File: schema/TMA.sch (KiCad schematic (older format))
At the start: 20 parts, among them U1 BMP280, U2 BMI160

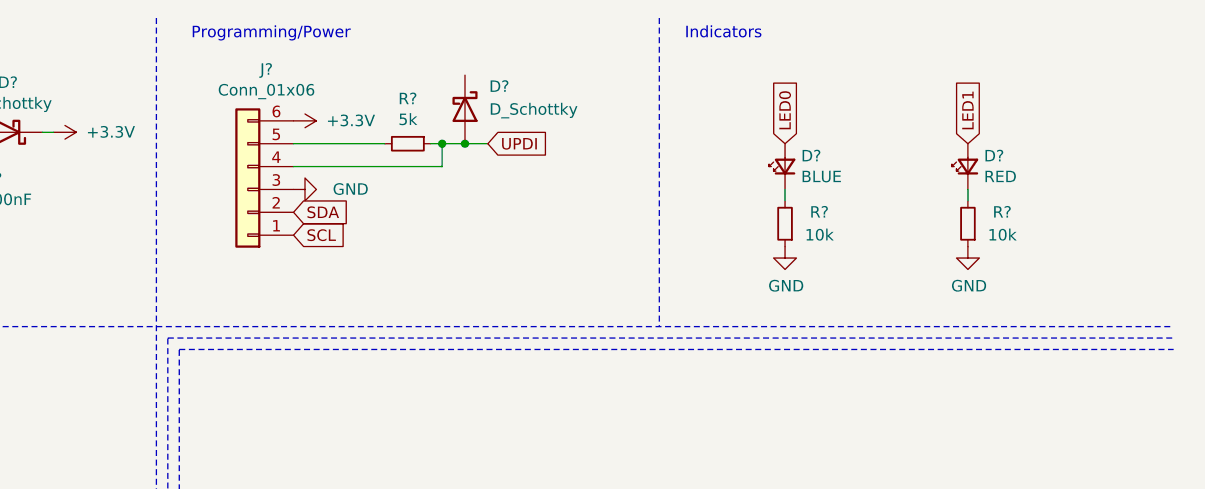
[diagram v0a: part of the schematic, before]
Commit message: Add pullups and mode switch, closes #1 and #2.
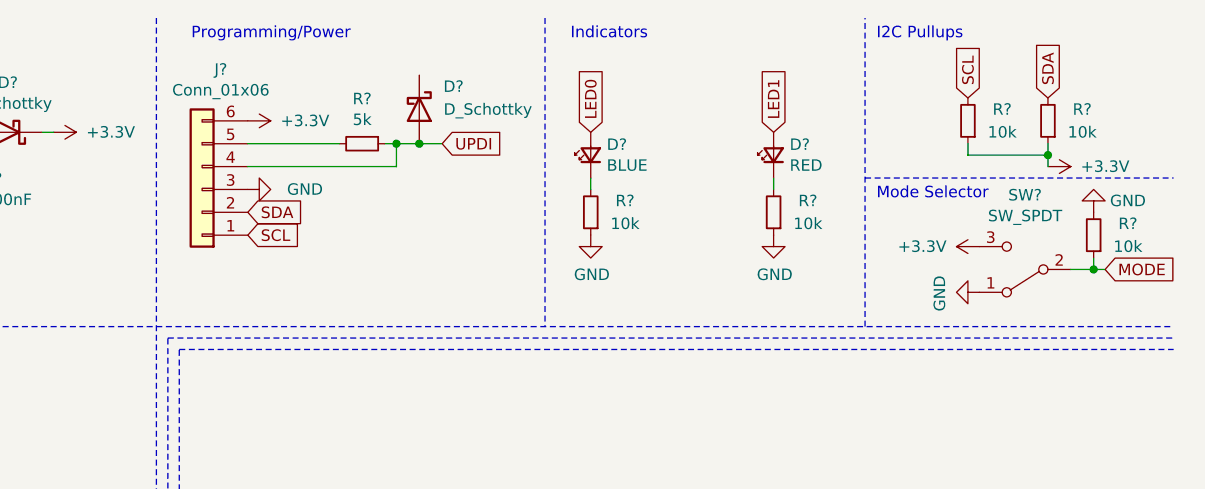
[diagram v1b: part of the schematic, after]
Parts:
- added R? (x3): 10k, symbol Device:R_Small
- added SW?: SW_SPDT, symbol Switch:SW_SPDT
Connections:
- net +3V3: now also R?.1, R?.1, SW?.3 (C)
- net GND: now also R?.2, SW?.1 (A)
- net SCL: now also R?.2
- net SDA: now also R?.2
- new net MODE: R?.1, SW?.2 (B)
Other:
- note added: "I2C Pullups\n"
- note added: "Mode Selector"
- moved on the sheet: D?, J?, R?
